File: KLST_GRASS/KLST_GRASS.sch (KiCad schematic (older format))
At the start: 19 parts, among them J2 PERIPHERALS, J3 USB_A, J5 USB_B_Micro, U1 TP4056, X1 KLST_GRASS--graphics, X2 KLST_GRASS--icon, X3 KLST_GRASS--wolf

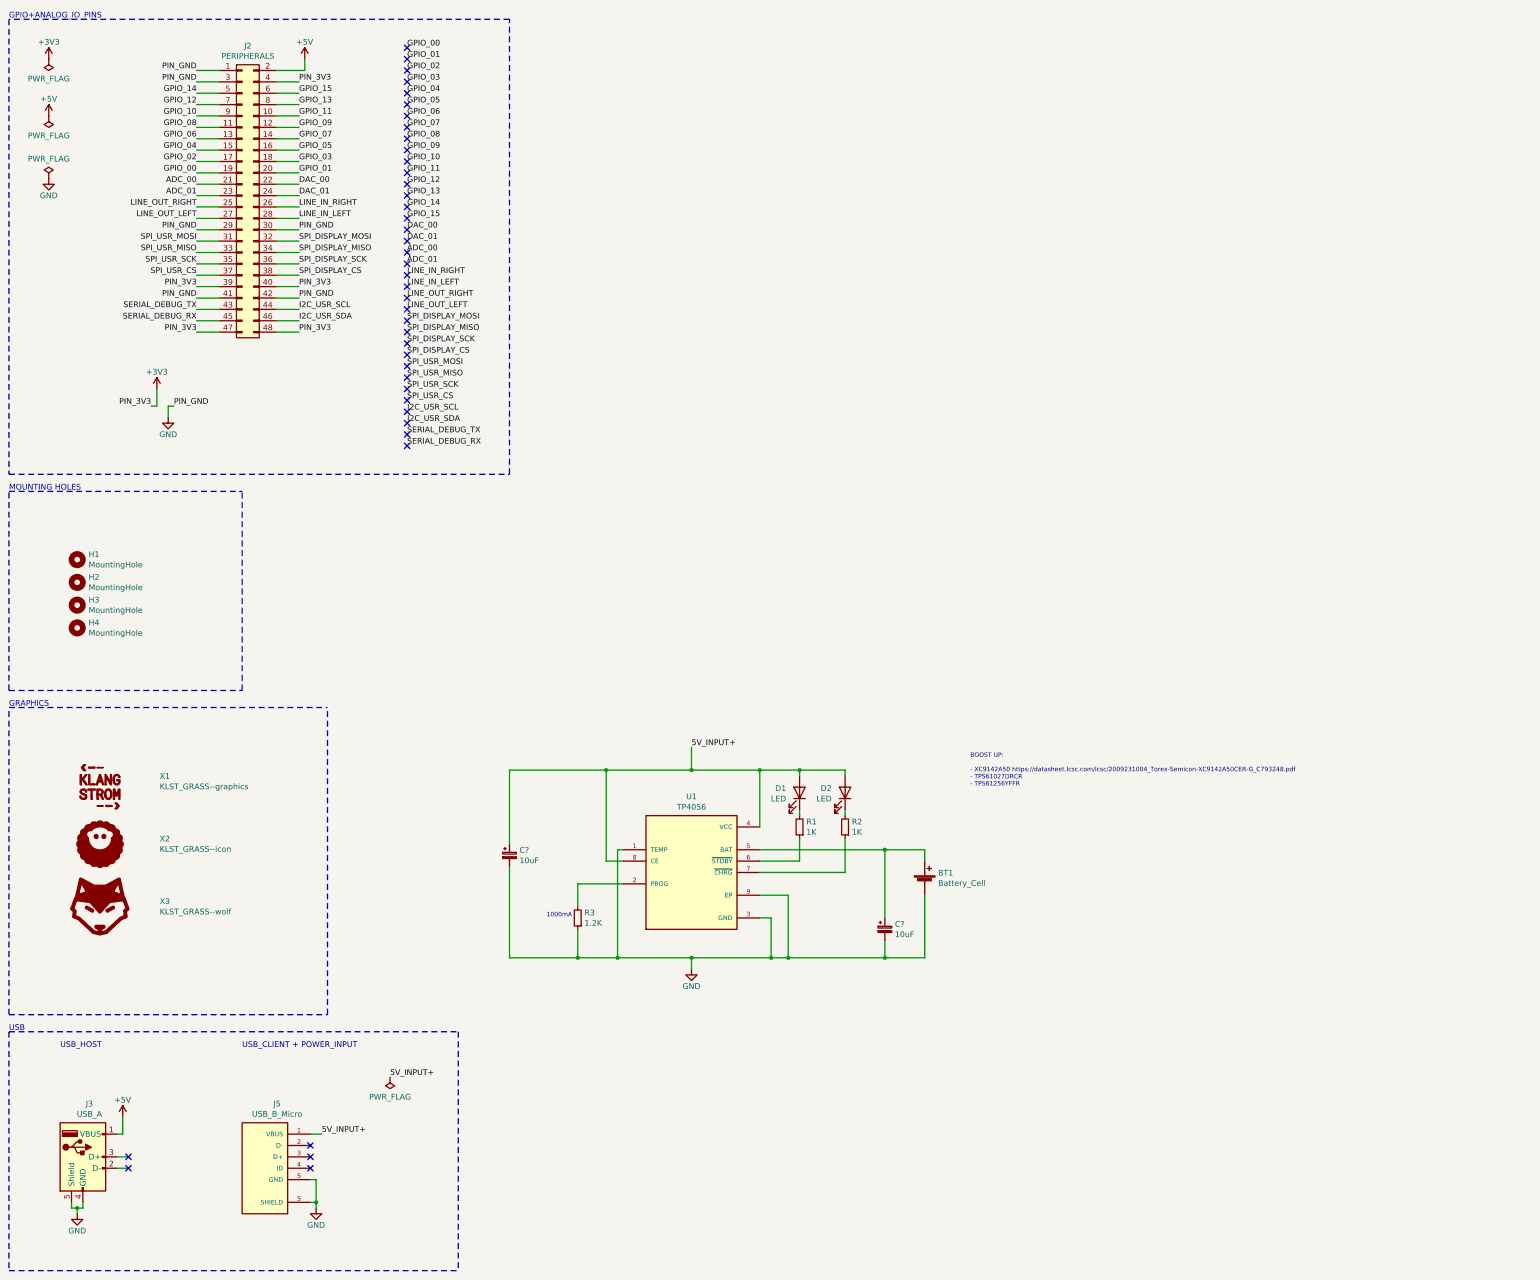
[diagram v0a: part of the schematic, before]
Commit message: finished schematics, started PCB design
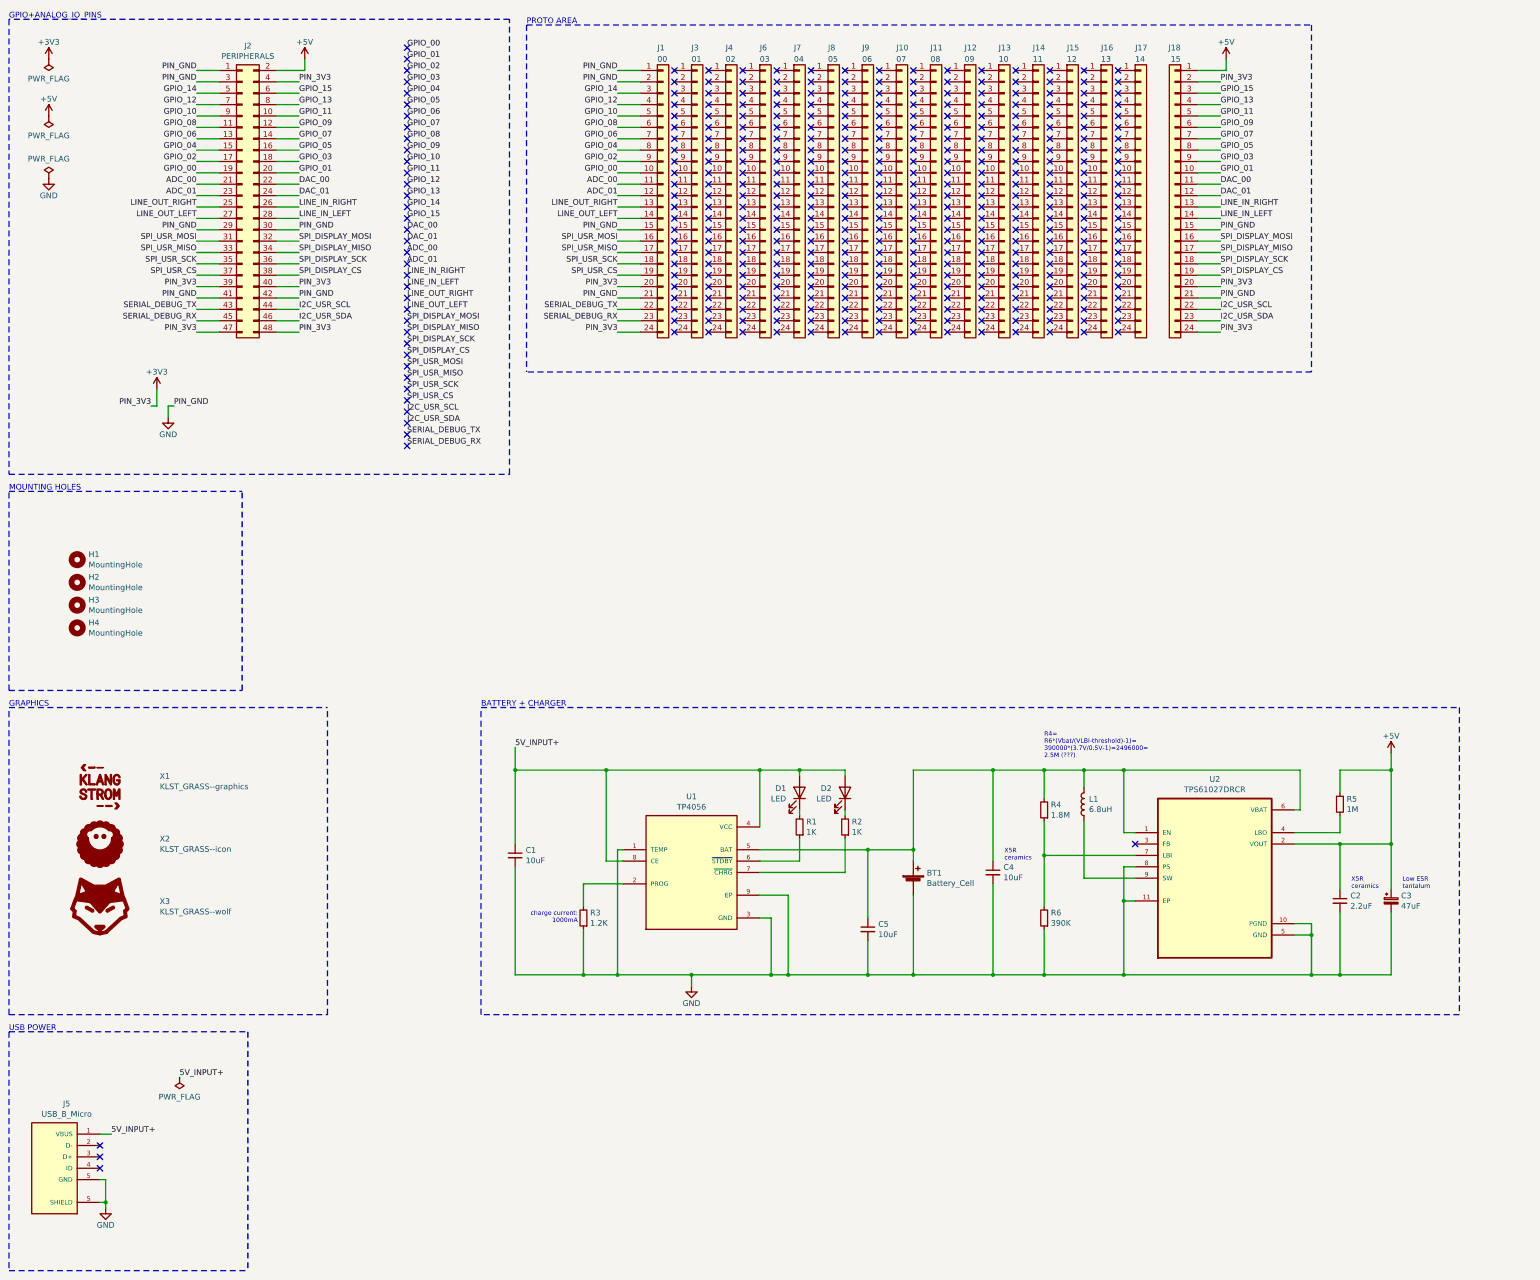
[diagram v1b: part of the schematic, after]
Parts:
- removed C? (x2): 10uF, symbol Device:CP_Small
- removed J3: USB_A, Connector_USB:USB_A_Molex_67643_Horizontal, symbol Connector:USB_A
- added C1, C4, C5: 10uF, Capacitor_SMD:C_0603_1608Metric_Pad1.08x0.95mm_HandSolder, symbol Device:C_Small
- added C2: 2.2uF, Capacitor_SMD:C_0603_1608Metric_Pad1.08x0.95mm_HandSolder, symbol Device:C_Small
- added C3: 47uF, Capacitor_Tantalum_SMD:CP_EIA-3216-18_Kemet-A_Pad1.58x1.35mm_HandSolder, symbol Device:CP_Small
- added J1: 00, Connector_PinHeader_2.54mm:PinHeader_1x24_P2.54mm_Vertical, symbol Connector_Generic:Conn_01x24
- added J10: 07, Connector_PinHeader_2.54mm:PinHeader_1x24_P2.54mm_Vertical, symbol Connector_Generic:Conn_01x24
- added J11: 08, Connector_PinHeader_2.54mm:PinHeader_1x24_P2.54mm_Vertical, symbol Connector_Generic:Conn_01x24
- added J12: 09, Connector_PinHeader_2.54mm:PinHeader_1x24_P2.54mm_Vertical, symbol Connector_Generic:Conn_01x24
- added J13: 10, Connector_PinHeader_2.54mm:PinHeader_1x24_P2.54mm_Vertical, symbol Connector_Generic:Conn_01x24
- added J14: 11, Connector_PinHeader_2.54mm:PinHeader_1x24_P2.54mm_Vertical, symbol Connector_Generic:Conn_01x24
- added J15: 12, Connector_PinHeader_2.54mm:PinHeader_1x24_P2.54mm_Vertical, symbol Connector_Generic:Conn_01x24
- added J16: 13, Connector_PinHeader_2.54mm:PinHeader_1x24_P2.54mm_Vertical, symbol Connector_Generic:Conn_01x24
- added J17: 14, Connector_PinHeader_2.54mm:PinHeader_1x24_P2.54mm_Vertical, symbol Connector_Generic:Conn_01x24
- added J18: 15, Connector_PinHeader_2.54mm:PinHeader_1x24_P2.54mm_Vertical, symbol Connector_Generic:Conn_01x24
- added J3: 01, Connector_PinHeader_2.54mm:PinHeader_1x24_P2.54mm_Vertical, symbol Connector_Generic:Conn_01x24
- added J4: 02, Connector_PinHeader_2.54mm:PinHeader_1x24_P2.54mm_Vertical, symbol Connector_Generic:Conn_01x24
- added J6: 03, Connector_PinHeader_2.54mm:PinHeader_1x24_P2.54mm_Vertical, symbol Connector_Generic:Conn_01x24
- added J7: 04, Connector_PinHeader_2.54mm:PinHeader_1x24_P2.54mm_Vertical, symbol Connector_Generic:Conn_01x24
- added J8: 05, Connector_PinHeader_2.54mm:PinHeader_1x24_P2.54mm_Vertical, symbol Connector_Generic:Conn_01x24
- added J9: 06, Connector_PinHeader_2.54mm:PinHeader_1x24_P2.54mm_Vertical, symbol Connector_Generic:Conn_01x24
- added L1: 6.8uH, Inductor_SMD:L_Bourns-SRN4018, symbol Device:L
- added R4: 1.8M, Resistor_SMD:R_0805_2012Metric_Pad1.20x1.40mm_HandSolder, symbol Device:R_Small
- added R5: 1M, Resistor_SMD:R_0805_2012Metric_Pad1.20x1.40mm_HandSolder, symbol Device:R_Small
- added R6: 390K, Resistor_SMD:R_0805_2012Metric_Pad1.20x1.40mm_HandSolder, symbol Device:R_Small
- added U2: TPS61027DRCR, KLST_GRASS:TPS61027DRCR, symbol TPS61027DRCR:TPS61027DRCR
- BT1: footprint Battery:BatteryHolder_MPD_BH-18650-PC2 -> KLST_GRASS:Keystone Electronics - PC Battery Clip #54
- H1, H2, H3, H4: Extended Part - -> (none)
- J2: footprint Connector_PinHeader_2.54mm:PinHeader_2x24_P2.54mm_Vertical_SMD -> Connector_PinHeader_2.54mm:PinHeader_2x24_P2.54mm_Vertical
- R3: JLCPCB Part # C17513 -> C17379; MFR.Part # 0805W8F1001T5E -> 0805W8F1201T5E
- U1: Extended Part (none) -> -; JLCPCB Part # (none) -> C16581; MFR.Part # (none) -> TP4056-42-ESOP8
- X1, X2, X3: JLCPCB Part # (none) -> DNF; MFR.Part # (none) -> DNF
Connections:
- net +3V3: now also J1.20 (Pin_20), J1.24 (Pin_24), J18.2 (Pin_2), J18.20 (Pin_20), J18.24 (Pin_24)
- net +5V: now also C2.1, C3.1, J18.1 (Pin_1), R5.1, U2.2 (VOUT)
- net 5V_INPUT+: now also C1.1
- net ADC_00: now also J1.11 (Pin_11)
- net ADC_01: now also J1.12 (Pin_12)
- net DAC_00: now also J18.11 (Pin_11)
- net DAC_01: now also J18.12 (Pin_12)
- net GND: now also C1.2, C2.2, C3.2, C4.2, C5.2, J1.1 (Pin_1), J1.15 (Pin_15), J1.2 (Pin_2), J1.21 (Pin_21), J18.15 (Pin_15), J18.21 (Pin_21), R6.1, U2.10 (PGND), U2.11 (EP), U2.5 (GND), U2.8 (PS)
- net GPIO_00: now also J1.10 (Pin_10)
- net GPIO_01: now also J18.10 (Pin_10)
- net GPIO_02: now also J1.9 (Pin_9)
- net GPIO_03: now also J18.9 (Pin_9)
- net GPIO_04: now also J1.8 (Pin_8)
- net GPIO_05: now also J18.8 (Pin_8)
- net GPIO_06: now also J1.7 (Pin_7)
- net GPIO_07: now also J18.7 (Pin_7)
- net GPIO_08: now also J1.6 (Pin_6)
- net GPIO_09: now also J18.6 (Pin_6)
- net GPIO_10: now also J1.5 (Pin_5)
- net GPIO_11: now also J18.5 (Pin_5)
- net GPIO_12: now also J1.4 (Pin_4)
- net GPIO_13: now also J18.4 (Pin_4)
- net GPIO_14: now also J1.3 (Pin_3)
- net GPIO_15: now also J18.3 (Pin_3)
- net I2C_USR_SCL: now also J18.22 (Pin_22)
- net I2C_USR_SDA: now also J18.23 (Pin_23)
- net LINE_IN_LEFT: now also J18.14 (Pin_14)
- net LINE_IN_RIGHT: now also J18.13 (Pin_13)
- net LINE_OUT_LEFT: now also J1.14 (Pin_14)
- net LINE_OUT_RIGHT: now also J1.13 (Pin_13)
- net SERIAL_DEBUG_RX: now also J1.23 (Pin_23)
- net SERIAL_DEBUG_TX: now also J1.22 (Pin_22)
- net SPI_DISPLAY_CS: now also J18.19 (Pin_19)
- net SPI_DISPLAY_MISO: now also J18.17 (Pin_17)
- net SPI_DISPLAY_MOSI: now also J18.16 (Pin_16)
- net SPI_DISPLAY_SCK: now also J18.18 (Pin_18)
- net SPI_USR_CS: now also J1.19 (Pin_19)
- net SPI_USR_MISO: now also J1.17 (Pin_17)
- net SPI_USR_MOSI: now also J1.16 (Pin_16)
- net SPI_USR_SCK: now also J1.18 (Pin_18)
- net at BT1.1 (+), U1.5 (BAT): now also C4.1, C5.1, L1.2, R4.2, U2.1 (EN), U2.6 (VBAT)
- new net: R5.2, U2.4 (LBO)
- new net: R4.1, R6.2, U2.7 (LBI)
- new net: L1.1, U2.9 (SW)
- no-connect marks 41 -> 376
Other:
- note added: "BATTERY + CHARGER"
- note added: "Low ESR\ntantalum"
- note added: "PROTO AREA"
- note added: "R4=\nR6*(Vbat/(VLBI-threshold)-1)=\n390000*(3.7V/0.5V-1)=2496000=\n2.5M (???)"
- note added: "USB POWER"
- note added: "X5R\nceramics"
- note added: "charge current:\n1000mA"
- note removed: "1000mA"
- note removed: "BOOST UP:\n\n- XC9142A50 https://datasheet.lcsc.com/lcsc/2009231004_Torex-Semicon-XC9142A50CER-G_C793248.pdf\n- TPS61027DRCR \n- TPS61256YFFR"
- note removed: "USB"
- note removed: "USB_CLIENT + POWER_INPUT"
- note removed: "USB_HOST"
- moved on the sheet: BT1, J5, R3
